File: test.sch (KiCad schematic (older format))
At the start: 20 parts, among them P1 CONN_02X20, P10 CONN_01X01, P11 CONN_01X04, P12 CONN_01X05, P13 CONN_01X05, P14 CONN_01X05, P15 CONN_01X04, P16 CONN_01X04, P2 CONN_02X04, P3 CONN_01X04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

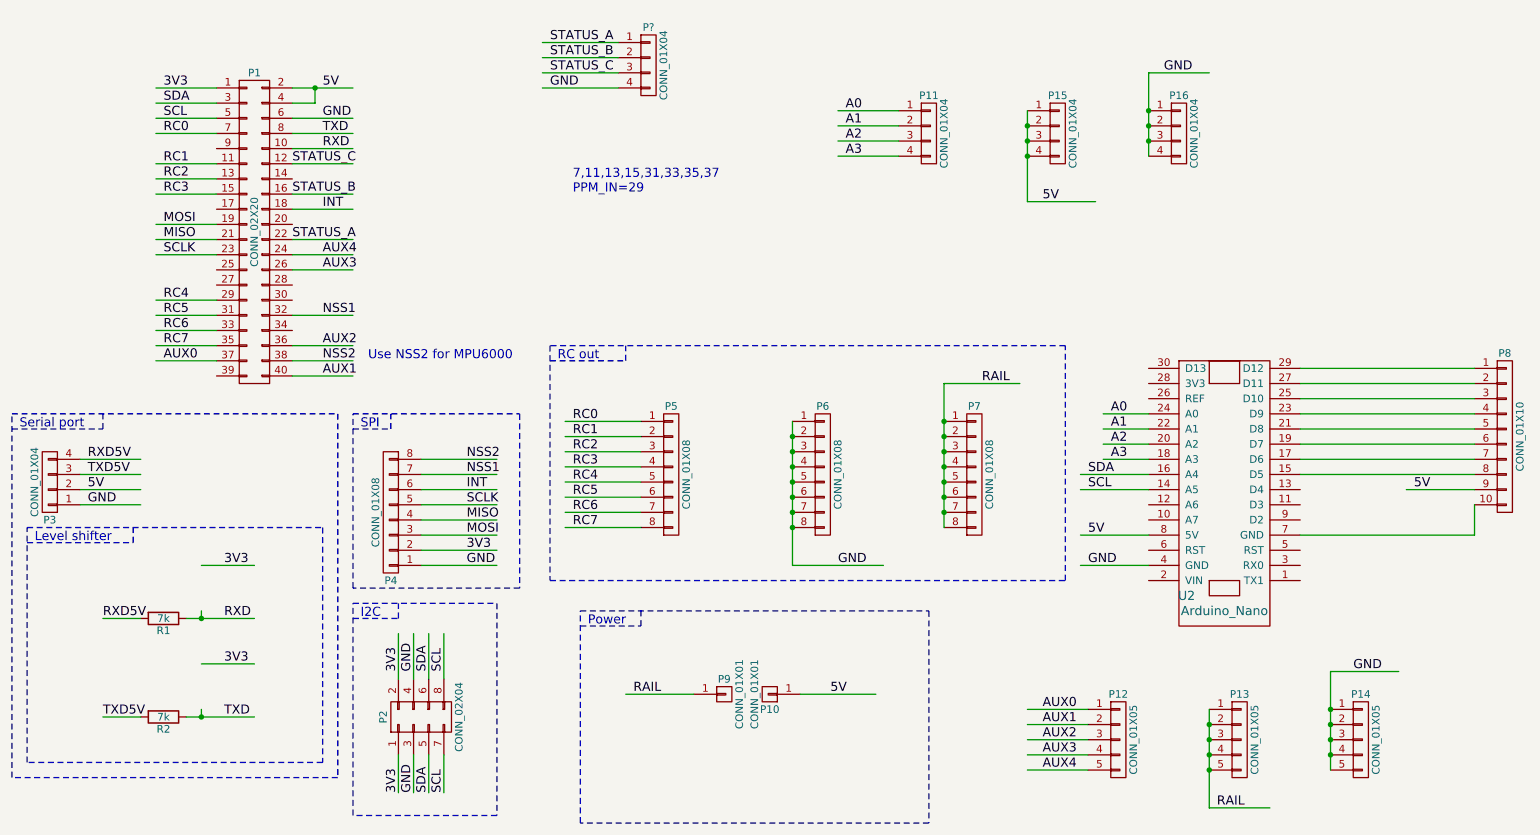
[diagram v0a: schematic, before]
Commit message: Input channel count increased in hardware, but not in software
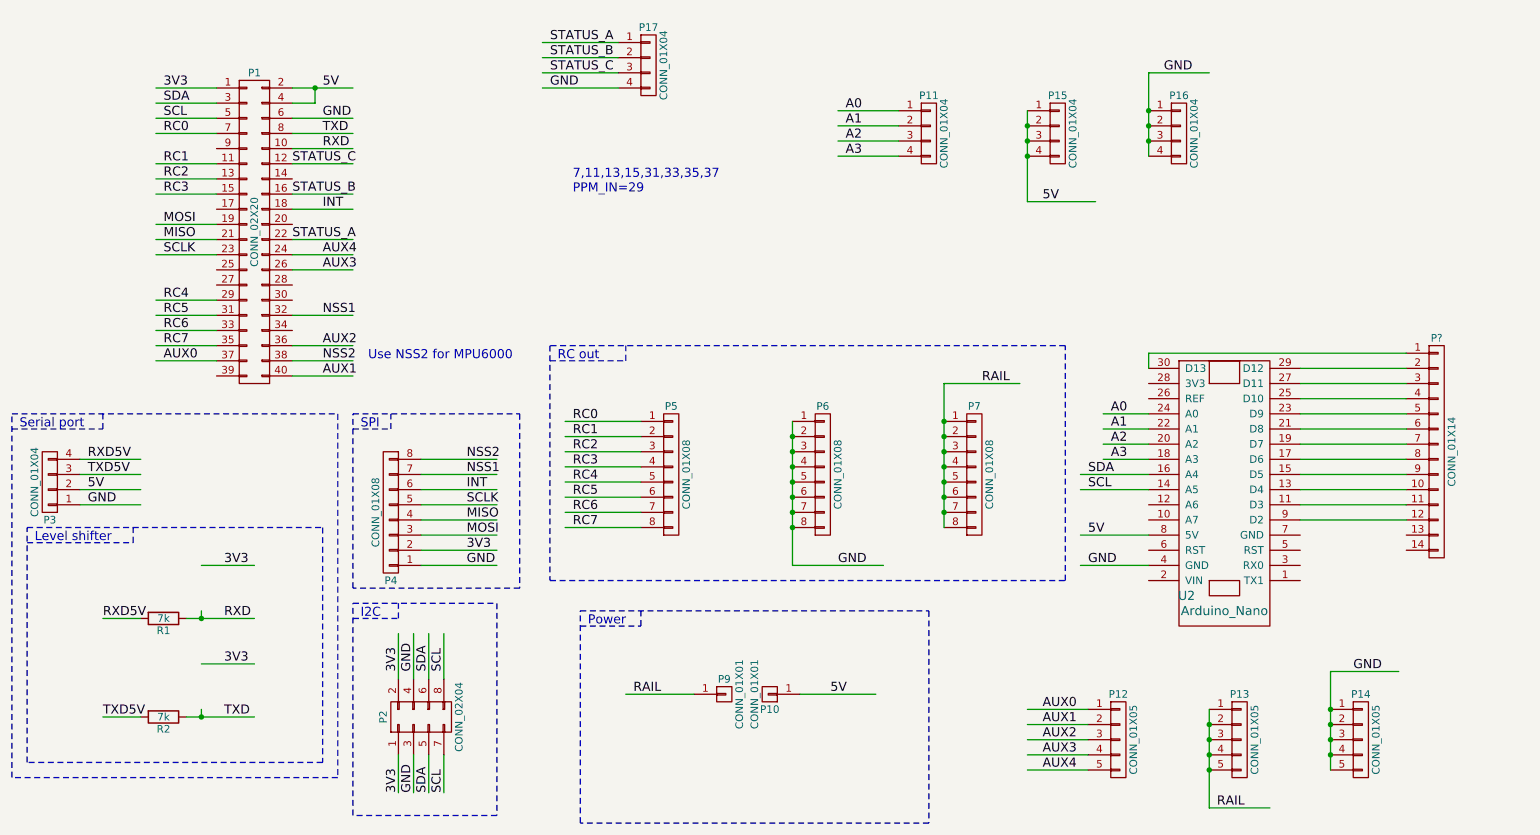
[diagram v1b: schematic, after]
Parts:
- removed P8: CONN_01X10, Pin_Headers:Pin_Header_Straight_1x10, symbol CONN_01X10
- added P?: CONN_01X14, symbol CONN_01X14
- P17: renamed from P?; footprint (none) -> Pin_Headers:Pin_Header_Straight_1x04
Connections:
- wire segments 113 -> 115

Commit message: Status leds added to hardware
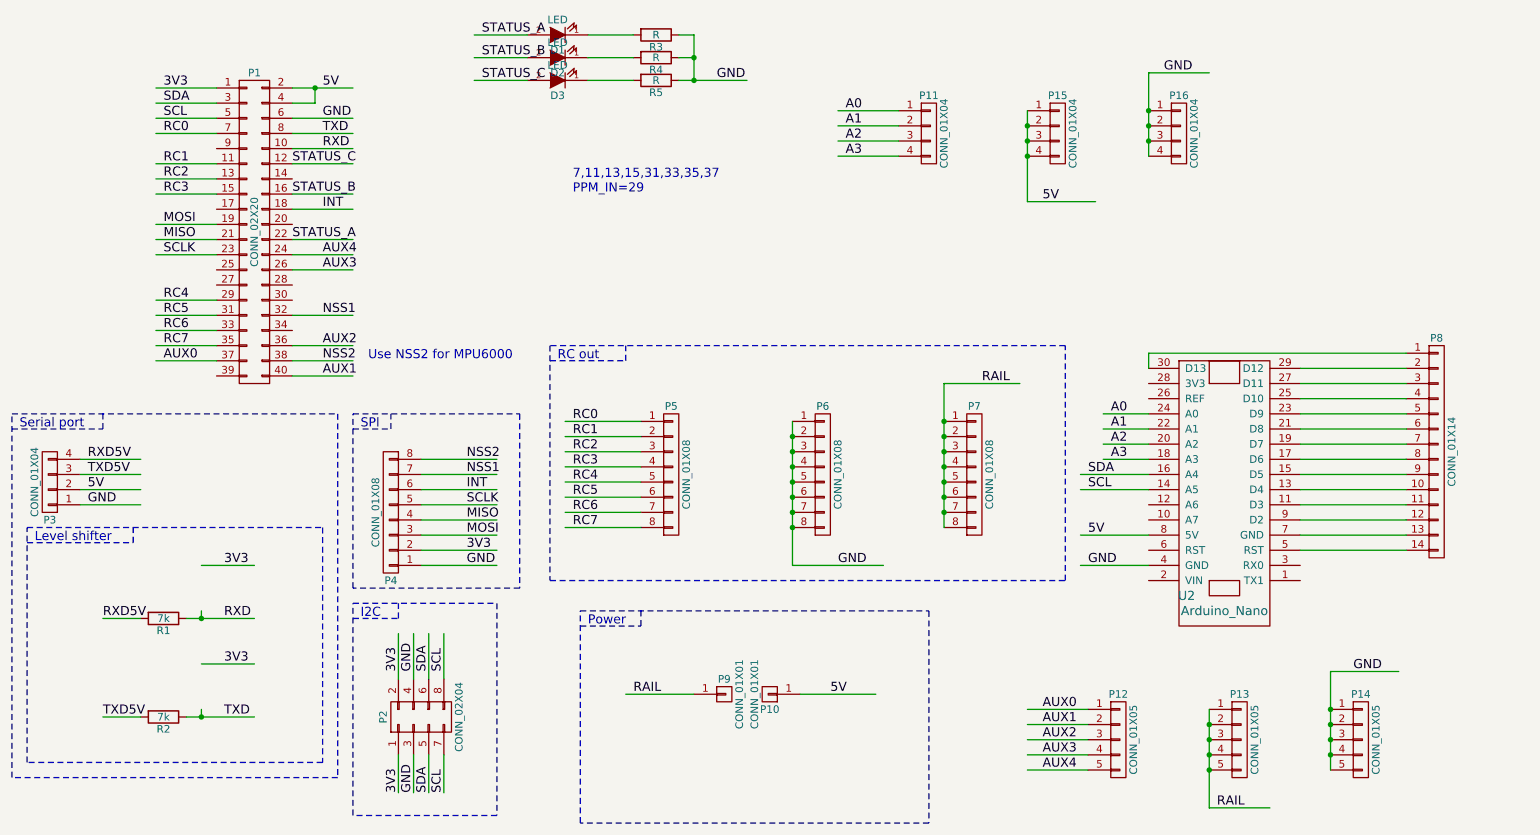
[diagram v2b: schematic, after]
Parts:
- removed P17: CONN_01X04, Pin_Headers:Pin_Header_Straight_1x04, symbol CONN_01X04
- added D1, D2, D3: LED, LEDs:LED-3MM, symbol LED
- added R3, R4, R5: R, Resistors_SMD:R_0805_HandSoldering, symbol R
- P8: renamed from P?; footprint (none) -> Pin_Headers:Pin_Header_Straight_1x14
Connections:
- wire segments 115 -> 123
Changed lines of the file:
@@
 A3
 $Comp
-L CONN_01X04 P17
-U 1 1 576935D8
-P 5350 1100
-F 0 "P17" H 5350 1350 50  0000 C CNN
-F 1 "CONN_01X04" V 5450 1100 50  0000 C CNN
-F 2 "Pin_Headers:Pin_Header_Straight_1x04" H 5350 1100 50  0001 C CNN
-F 3 "" H 5350 1100 50  0000 C CNN
-	1    5350 1100
-	1    0    0    -1
-$EndComp
-Text Label 4700 950  0    60   ~ 0
-STATUS_A
-Text Label 4700 1050 0    60   ~ 0
-STATUS_B
-Text Label 4700 1150 0    60   ~ 0
-STATUS_C
-Text Label 4700 1250 0    60   ~ 0
-GND
-$Comp
-L CONN_01X14 P?
+L CONN_01X14 P8
 U 1 1 57693CC8
 P 10550 3650
-F 0 "P?" H 10550 4400 50  0000 C CNN
+F 0 "P8" H 10550 4400 50  0000 C CNN
 F 1 "CONN_01X14" V 10650 3650 50  0000 C CNN
-F 2 "" H 10550 3650 50  0000 C CNN
+F 2 "Pin_Headers:Pin_Header_Straight_1x14" H 10550 3650 50  0001 C CNN
 F 3 "" H 10550 3650 50  0000 C CNN
 	1    10550 3650
@@
 	7000 1700 6600 1700
 Wire Wire Line
-	5150 950  4650 950
-Wire Wire Line
-	5150 1050 4650 1050
-Wire Wire Line
-	5150 1150 4650 1150
-Wire Wire Line
-	5150 1250 4650 1250
-Wire Wire Line
 	9650 4100 10350 4100
 Wire Wire Line
@@
 Wire Wire Line
 	8650 3000 8650 3100
+Wire Wire Line
+	9650 4200 10350 4200
+Wire Wire Line
+	10350 4300 9650 4300
+$Comp
+L LED D1
+U 1 1 5769062A
+P 4750 900
+F 0 "D1" H 4750 1000 50  0000 C CNN
+F 1 "LED" H 4750 800 50  0000 C CNN
+F 2 "LEDs:LED-3MM" H 4750 900 50  0001 C CNN
+F 3 "" H 4750 900 50  0000 C CNN
+	1    4750 900
+	-1   0    0    1
+$EndComp
+$Comp
+L LED D2
+U 1 1 57690763
+P 4750 1050
+F 0 "D2" H 4750 1150 50  0000 C CNN
+F 1 "LED" H 4750 950 50  0000 C CNN
+F 2 "LEDs:LED-3MM" H 4750 1050 50  0001 C CNN
+F 3 "" H 4750 1050 50  0000 C CNN
+	1    4750 1050
+	-1   0    0    1
+$EndComp
+$Comp
+L LED D3
+U 1 1 576907A8
+P 4750 1200
+F 0 "D3" H 4750 1300 50  0000 C CNN
+F 1 "LED" H 4750 1100 50  0000 C CNN
+F 2 "LEDs:LED-3MM" H 4750 1200 50  0001 C CNN
+F 3 "" H 4750 1200 50  0000 C CNN
+	1    4750 1200
+	-1   0    0    1
+$EndComp
+$Comp
+L R R3
+U 1 1 57690955
+P 5400 900
+F 0 "R3" V 5480 900 50  0000 C CNN
+F 1 "R" V 5400 900 50  0000 C CNN
+F 2 "Resistors_SMD:R_0805_HandSoldering" V 5330 900 50  0001 C CNN
+F 3 "" H 5400 900 50  0000 C CNN
+	1    5400 900
+	0    1    1    0
+$EndComp
+$Comp
+L R R4
+U 1 1 576909DA
+P 5400 1050
+F 0 "R4" V 5480 1050 50  0000 C CNN
+F 1 "R" V 5400 1050 50  0000 C CNN
+F 2 "Resistors_SMD:R_0805_HandSoldering" V 5330 1050 50  0001 C CNN
+F 3 "" H 5400 1050 50  0000 C CNN
+	1    5400 1050
+	0    1    1    0
+$EndComp
+$Comp
+L R R5
+U 1 1 57690A25
+P 5400 1200
+F 0 "R5" V 5480 1200 50  0000 C CNN
+F 1 "R" V 5400 1200 50  0000 C CNN
+F 2 "Resistors_SMD:R_0805_HandSoldering" V 5330 1200 50  0001 C CNN
+F 3 "" H 5400 1200 50  0000 C CNN
+	1    5400 1200
+	0    1    1    0
+$EndComp
+Wire Wire Line
+	4950 900  5250 900
+Wire Wire Line
+	4950 1050 5250 1050
+Wire Wire Line
+	5250 1200 4950 1200
+Wire Wire Line
+	5550 900  5650 900
+Wire Wire Line
+	5650 900  5650 1200
+Wire Wire Line
+	5650 1050 5550 1050
+Wire Wire Line
+	5550 1200 6000 1200
+Connection ~ 5650 1050
+Connection ~ 5650 1200
+Text Label 5800 1200 0    60   ~ 0
+GND
+Wire Wire Line
+	4550 900  4200 900
+Wire Wire Line
+	4550 1050 4200 1050
+Wire Wire Line
+	4550 1200 4200 1200
+Text Label 4250 900  0    60   ~ 0
+STATUS_A
+Text Label 4250 1050 0    60   ~ 0
+STATUS_B
+Text Label 4250 1200 0    60   ~ 0
+STATUS_C
 $EndSCHEMATC

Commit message: Bugs fixed, added 5v connector
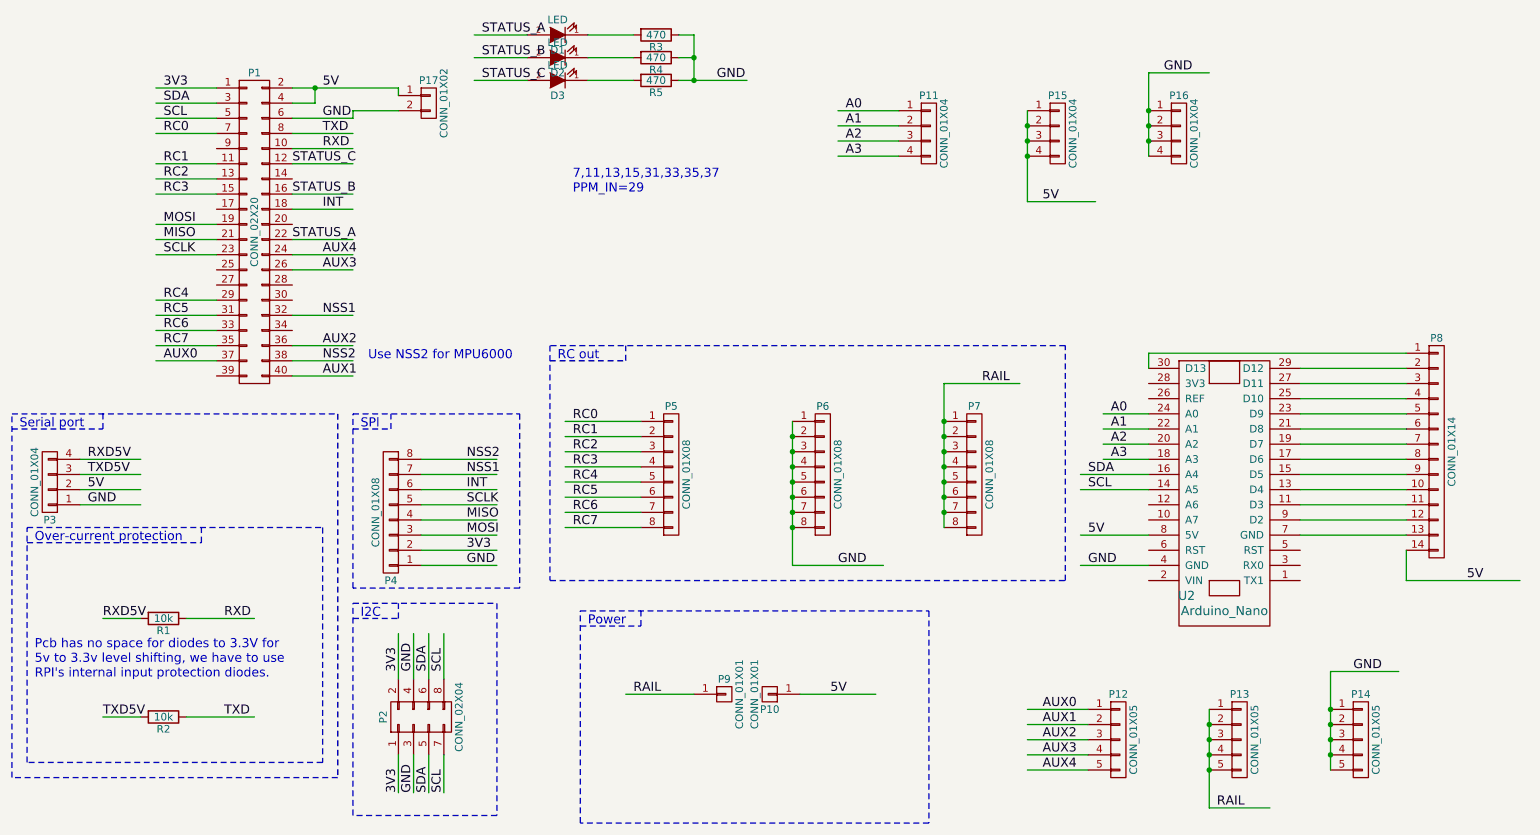
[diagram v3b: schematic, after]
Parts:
- added P17: CONN_01X02, Pin_Headers:Pin_Header_Straight_1x02, symbol CONN_01X02
- R1, R2: value 7k -> 10k
- R3, R4, R5: value R -> 470
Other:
- note added: "Over-current protection"
- note added: "Pcb has no space for diodes to 3.3V for\n5v to 3.3v level shifting, we have to use\nRPI's internal input protection diodes."
- note removed: "Level shifter"
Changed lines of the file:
@@
 LIBS:contrib
 LIBS:valves
-LIBS:test-cache
 EELAYER 25 0
 EELAYER END
@@
 P 2150 4750
 F 0 "R1" V 2230 4750 50  0000 C CNN
-F 1 "7k" V 2150 4750 50  0000 C CNN
+F 1 "10k" V 2150 4750 50  0000 C CNN
 F 2 "Resistors_SMD:R_0805_HandSoldering" V 2080 4750 50  0001 C CNN
 F 3 "" H 2150 4750 50  0000 C CNN
@@
 P 2150 5400
 F 0 "R2" V 2230 5400 50  0000 C CNN
-F 1 "7k" V 2150 5400 50  0000 C CNN
+F 1 "10k" V 2150 5400 50  0000 C CNN
 F 2 "Resistors_SMD:R_0805_HandSoldering" V 2080 5400 50  0001 C CNN
 F 3 "" H 2150 5400 50  0000 C CNN
@@
 	0    1    1    0
 $EndComp
-Text Label 2550 4400 0    60   ~ 0
-3V3
-Text Label 2550 5050 0    60   ~ 0
-3V3
 Text Label 2550 5400 0    60   ~ 0
 TXD
@@
 TXD5V
 Text Notes 1300 4250 0    60   ~ 0
-Level shifter
+Over-current protection
 Text Notes 1200 3500 0    60   ~ 0
 Serial port
@@
 	3000 3050 3400 3050
 Wire Wire Line
-	3000 1250 3400 1250
+	3000 1250 3700 1250
 Wire Wire Line
 	3150 1250 3150 1350
@@
 	2300 4750 2750 4750
 Wire Wire Line
-	2400 4750 2400 4700
-Connection ~ 2400 4750
-Wire Wire Line
-	2400 4400 2750 4400
-Wire Wire Line
 	2000 4750 1750 4750
 Wire Notes Line
@@
 	2300 5400 2750 5400
 Wire Wire Line
-	2400 5400 2400 5350
-Connection ~ 2400 5400
-Wire Wire Line
-	2400 5050 2750 5050
-Wire Wire Line
 	2000 5400 1750 5400
 Wire Notes Line
-	1250 4250 1950 4250
-Wire Notes Line
-	1950 4250 1950 4150
+	1250 4250 2400 4250
 Wire Notes Line
 	1150 3400 3300 3400
@@
 Wire Wire Line
 	9650 4200 10350 4200
-Wire Wire Line
-	10350 4300 9650 4300
 $Comp
 L LED D1
@@
 P 5400 900
 F 0 "R3" V 5480 900 50  0000 C CNN
-F 1 "R" V 5400 900 50  0000 C CNN
+F 1 "470" V 5400 900 50  0000 C CNN
 F 2 "Resistors_SMD:R_0805_HandSoldering" V 5330 900 50  0001 C CNN
 F 3 "" H 5400 900 50  0000 C CNN
@@
 P 5400 1050
 F 0 "R4" V 5480 1050 50  0000 C CNN
-F 1 "R" V 5400 1050 50  0000 C CNN
+F 1 "470" V 5400 1050 50  0000 C CNN
 F 2 "Resistors_SMD:R_0805_HandSoldering" V 5330 1050 50  0001 C CNN
 F 3 "" H 5400 1050 50  0000 C CNN
@@
 P 5400 1200
 F 0 "R5" V 5480 1200 50  0000 C CNN
-F 1 "R" V 5400 1200 50  0000 C CNN
+F 1 "470" V 5400 1200 50  0000 C CNN
 F 2 "Resistors_SMD:R_0805_HandSoldering" V 5330 1200 50  0001 C CNN
 F 3 "" H 5400 1200 50  0000 C CNN
@@
 Text Label 4250 1200 0    60   ~ 0
 STATUS_C
+Wire Wire Line
+	10350 4300 10350 4500
+Wire Wire Line
+	10350 4500 11100 4500
+Text Label 10750 4500 0    60   ~ 0
+5V
+Wire Notes Line
+	2400 4250 2400 4150
+Text Notes 1300 5150 0    60   ~ 0
+Pcb has no space for diodes to 3.3V for\n5v to 3.3v level shifting, we have to use\nRPI's internal input protection diodes.
+$Comp
+L CONN_01X02 P17
+U 1 1 576958DC
+P 3900 1350
+F 0 "P17" H 3900 1500 50  0000 C CNN
+F 1 "CONN_01X02" V 4000 1350 50  0000 C CNN
+F 2 "Pin_Headers:Pin_Header_Straight_1x02" H 3900 1350 50  0001 C CNN
+F 3 "" H 3900 1350 50  0000 C CNN
+	1    3900 1350
+	1    0    0    -1
+$EndComp
+Wire Wire Line
+	3700 1250 3700 1300
+Wire Wire Line
+	3700 1400 3400 1400
+Wire Wire Line
+	3400 1400 3400 1450
 $EndSCHEMATC

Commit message: Added board render
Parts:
- added D5: LED, LEDs:LED-3MM, symbol LED
- added R7: R, Resistors_SMD:R_0805_HandSoldering, symbol R
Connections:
- net labels added: OK, RCOK
- wire segments 123 -> 128
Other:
- note added: "7,11,13,15,29,31,33,35,37,40,36,26,24"
- note removed: "7,11,13,15,31,33,35,37\nPPM_IN=29"
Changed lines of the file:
@@
 LIBS:contrib
 LIBS:valves
+LIBS:test-cache
 EELAYER 25 0
 EELAYER END
@@
 Text Label 2150 1550 0    60   ~ 0
 RC0
-Text Notes 4850 1950 0    60   ~ 0
-7,11,13,15,31,33,35,37\nPPM_IN=29
 Text Label 2150 1750 0    60   ~ 0
 RC1
@@
 Wire Wire Line
 	3400 1400 3400 1450
+Text Notes 4200 2300 0    60   ~ 0
+7,11,13,15,29,31,33,35,37,40,36,26,24
+Wire Wire Line
+	8650 4100 8200 4100
+Wire Wire Line
+	8650 4000 8200 4000
+Text Label 8250 4100 0    60   ~ 0
+RCOK
+Text Label 8250 4000 0    60   ~ 0
+OK
+$Comp
+L LED D5
+U 1 1 5769A8C2
+P 4750 1700
+F 0 "D5" H 4750 1800 50  0000 C CNN
+F 1 "LED" H 4750 1600 50  0000 C CNN
+F 2 "LEDs:LED-3MM" H 4750 1700 50  0001 C CNN
+F 3 "" H 4750 1700 50  0000 C CNN
+	1    4750 1700
+	-1   0    0    1
+$EndComp
+Wire Wire Line
+	4550 1700 4250 1700
+Wire Wire Line
+	4950 1700 5350 1700
+$Comp
+L R R7
+U 1 1 5769C814
+P 5500 1700
+F 0 "R7" V 5580 1700 50  0000 C CNN
+F 1 "R" V 5500 1700 50  0000 C CNN
+F 2 "Resistors_SMD:R_0805_HandSoldering" V 5430 1700 50  0001 C CNN
+F 3 "" H 5500 1700 50  0000 C CNN
+	1    5500 1700
+	0    1    1    0
+$EndComp
+Wire Wire Line
+	5650 1700 6000 1700
+Text Label 5800 1700 0    60   ~ 0
+GND
+Text Label 4300 1700 0    60   ~ 0
+RCOK
 $EndSCHEMATC
